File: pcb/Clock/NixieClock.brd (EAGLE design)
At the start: 108.4 x 46.5 mm, 47 parts, among them IC1 74141N, IC2 MEGA8-P, IC3 7805L, J1 DC-8N, Q1 IRF710, Q2 32kHz

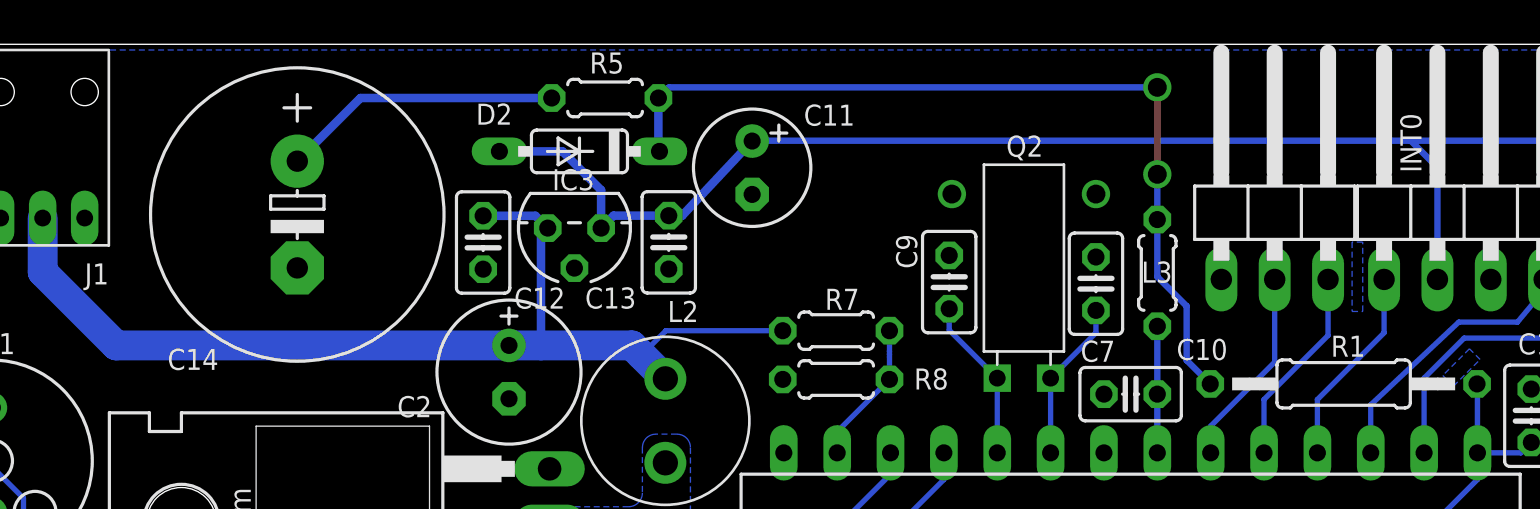
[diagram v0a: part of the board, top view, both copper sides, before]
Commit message: Replaced backup capacitor with a CR1220 battery holder.
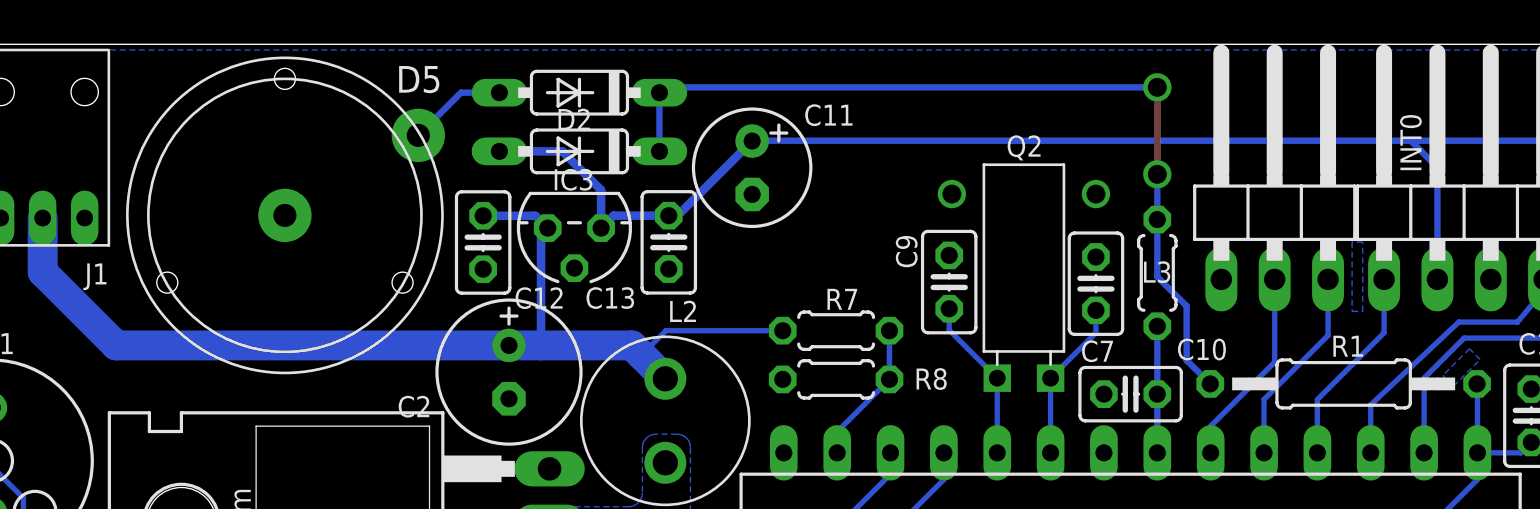
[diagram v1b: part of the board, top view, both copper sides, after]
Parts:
- removed C14: 0.1F, rcl:E5-13
- removed R5: 100, rcl:0204/5
- added D5: BAT85, diode:DO35-7
- added U$3: BAT1220THT, WB:1220
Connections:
- net GND: now also U$3.-; no longer C14.-
- net N$3: now also D5.A, U$3.+; no longer C14.+, R5.1
- net UC_VCC: now also D5.C; no longer R5.2
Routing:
- net N$3: track 13.4 -> 4.70 mm
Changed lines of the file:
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@@
 <?xml version="1.0" encoding="utf-8"?>
 <!DOCTYPE eagle SYSTEM "eagle.dtd">
-<eagle version="6.3">
+<eagle version="6.6.0">
 <drawing>
 <settings>
@@
 <attribute name="VALUE" x="50.927" y="45.847" size="1" layer="27" ratio="10" rot="R270"/>
 </element>
-<element name="C14" library="rcl" package="E5-13" value="0.1F" x="22.687" y="46.7775" smashed="yes" rot="R270">
-<attribute name="NAME" x="18.9391" y="40.3812" size="1" layer="25" ratio="10" rot="R180"/>
-<attribute name="VALUE" x="18.75" y="51.3495" size="1" layer="27" ratio="10" rot="R270"/>
-</element>
 <element name="D2" library="diode" package="DO35-7" value="BAT85" x="36.1188" y="49.784" smashed="yes" rot="R180">
-<attribute name="NAME" x="31.1912" y="51.054" size="1" layer="25" ratio="10"/>
+<attribute name="NAME" x="35.0012" y="50.8" size="1" layer="25" ratio="10"/>
 <attribute name="VALUE" x="34.5694" y="54.4322" size="1" layer="27" ratio="10" rot="R180"/>
 </element>
@@
 <attribute name="NAME" x="23.1394" y="28.321" size="1" layer="25" ratio="10" rot="R90"/>
 <attribute name="VALUE" x="25.8064" y="28.194" size="1" layer="27" ratio="10" rot="R90"/>
-</element>
-<element name="R5" library="rcl" package="0204/5" value="100" x="37.338" y="52.324" smashed="yes">
-<attribute name="NAME" x="36.6014" y="53.4924" size="1" layer="25" ratio="10"/>
-<attribute name="VALUE" x="35.2044" y="50.0126" size="1" layer="27" ratio="10"/>
 </element>
 <element name="C5" library="Various" package="CAP_RADIAL" value="4.7uF/250V" x="22.352" y="18.034" smashed="yes" rot="R180"/>
@@
 </element>
 <element name="R9" library="rcl" package="0204/5" value="10" x="40.132" y="29.591"/>
+<element name="U$3" library="WB" package="1220" value="BAT1220THT" x="22.098" y="46.736" rot="R180"/>
+<element name="D5" library="diode" package="DO35-7" value="BAT85" x="36.1188" y="52.578" smashed="yes" rot="R180">
+<attribute name="NAME" x="27.3812" y="52.578" size="1.27" layer="25" ratio="10"/>
+<attribute name="VALUE" x="38.4048" y="55.245" size="1.27" layer="27" ratio="10" rot="R180"/>
+</element>
 </elements>
 <signals>
@@
 <wire x1="40.3705" y1="46.7236" x2="37.7417" y2="46.7236" width="0.4064" layer="16"/>
 <wire x1="37.7417" y1="46.7236" x2="37.1497" y2="46.1316" width="0.4064" layer="16"/>
-<wire x1="75.692" y1="50.292" x2="44.3226" y2="50.292" width="0.3048" layer="16"/>
-<wire x1="41.0082" y1="46.7236" x2="40.3705" y2="46.7236" width="0.4064" layer="16"/>
+<wire x1="75.692" y1="50.292" x2="44.3576" y2="50.292" width="0.3048" layer="16"/>
 <wire x1="37.1497" y1="46.1316" x2="37.1497" y2="47.9403" width="0.4064" layer="16"/>
 <wire x1="37.1497" y1="47.9403" x2="35.306" y2="49.784" width="0.4064" layer="16"/>
 <wire x1="35.306" y1="49.784" x2="32.3088" y2="49.784" width="0.4064" layer="16"/>
 <wire x1="89.281" y1="34.163" x2="86.741" y2="34.163" width="0.3048" layer="16"/>
-<wire x1="44.3226" y1="50.292" x2="44.3405" y2="50.2749" width="0.4064" layer="16"/>
-<wire x1="41.0082" y1="46.7236" x2="44.3405" y2="50.2749" width="0.4064" layer="16"/>
 <wire x1="84.6836" y1="28.321" x2="85.1916" y2="27.813" width="0.4064" layer="16"/>
 <wire x1="85.1916" y1="27.813" x2="88.011" y2="27.813" width="0.3048" layer="16"/>
@@
 <wire x1="83.9724" y1="23.876" x2="83.9724" y2="21.5392" width="0.3048" layer="16"/>
 <wire x1="83.9724" y1="21.5392" x2="84.074" y2="21.4376" width="0.3048" layer="16"/>
+<wire x1="44.3576" y1="50.292" x2="44.3405" y2="50.2749" width="0.3048" layer="16"/>
+<wire x1="40.3705" y1="46.7236" x2="40.7892" y2="46.7236" width="0.4064" layer="16"/>
+<wire x1="40.7892" y1="46.7236" x2="44.3405" y2="50.2749" width="0.4064" layer="16"/>
 </signal>
 <signal name="GND">
@@
 <contactref element="C4" pad="2"/>
 <contactref element="C11" pad="-"/>
-<contactref element="C14" pad="-"/>
 <wire x1="63.627" y1="24.765" x2="63.627" y2="27.813" width="0.6096" layer="16"/>
 <wire x1="63.627" y1="21.844" x2="63.627" y2="24.765" width="0.6096" layer="16"/>
@@
 <contactref element="D4" pad="A"/>
 <contactref element="R3" pad="1"/>
+<contactref element="U$3" pad="-"/>
 </signal>
 <signal name="N$10">
@@
 <contactref element="D2" pad="C"/>
 <contactref element="R1" pad="2"/>
-<contactref element="R5" pad="2"/>
-<wire x1="63.627" y1="52.832" x2="40.386" y2="52.832" width="0.3048" layer="16"/>
-<wire x1="40.386" y1="52.832" x2="39.878" y2="52.324" width="0.3048" layer="16"/>
-<wire x1="39.878" y1="52.324" x2="39.878" y2="50.0888" width="0.4064" layer="16"/>
-<wire x1="39.878" y1="50.0888" x2="39.9288" y2="49.784" width="0.4064" layer="16"/>
+<wire x1="63.627" y1="52.832" x2="40.1828" y2="52.832" width="0.3048" layer="16"/>
 <wire x1="63.6272" y1="46.5383" x2="63.6272" y2="43.8148" width="0.3048" layer="16"/>
 <wire x1="65.024" y1="39.8368" x2="65.024" y2="42.418" width="0.3048" layer="16"/>
@@
 <wire x1="63.627" y1="48.6918" x2="63.627" y2="52.832" width="0.3048" layer="1"/>
 <via x="63.627" y="52.832" extent="1-16" drill="0.9"/>
+<contactref element="D5" pad="C"/>
+<wire x1="40.1828" y1="52.832" x2="39.9288" y2="52.578" width="0.3048" layer="16"/>
+<wire x1="39.9288" y1="49.784" x2="39.9288" y2="52.578" width="0.3048" layer="16"/>
 </signal>
 <signal name="ANODE2">
@@
 <wire x1="48.387" y1="36.4404" x2="48.387" y2="35.433" width="0.254" layer="16"/>
 </signal>
-<signal name="N$3">
-<contactref element="R5" pad="1"/>
-<contactref element="C14" pad="+"/>
-<wire x1="34.798" y1="52.324" x2="25.6935" y2="52.324" width="0.4064" layer="16"/>
-<wire x1="25.6935" y1="52.324" x2="22.687" y2="49.3175" width="0.4064" layer="16"/>
-</signal>
 <signal name="RXD">
 <contactref element="IC2" pad="2"/>
@@
 <wire x1="37.592" y1="27.178" x2="37.592" y2="29.591" width="0.4064" layer="16"/>
 </signal>
+<signal name="N$3">
+<contactref element="U$3" pad="+"/>
+<contactref element="D5" pad="A"/>
+<wire x1="32.3088" y1="52.578" x2="30.48" y2="52.578" width="0.3048" layer="16"/>
+<wire x1="30.48" y1="52.578" x2="28.448" y2="50.546" width="0.3048" layer="16"/>
+</signal>
 </signals>

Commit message: Changed MOSFET from IRF710 to IRF740. Added part number for inductor
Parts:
- L2: value 330uH -> DLCW330 300uH/0.4A
- Q1: value IRF710 -> IRF740
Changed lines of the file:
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@@
 <attribute name="VALUE" x="17.4752" y="20.0152" size="1" layer="27" ratio="10" rot="R180"/>
 </element>
-<element name="L2" library="WB" package="MURATA-CHOKE-7-4" value="330uH" x="40.2082" y="36.957" smashed="yes" rot="R270">
+<element name="L2" library="WB" package="MURATA-CHOKE-7-4" value="DLCW330 300uH/0.4A" x="40.2082" y="36.957" smashed="yes" rot="R270">
 <attribute name="NAME" x="40.315" y="41.6602" size="1" layer="21"/>
 </element>
-<element name="Q1" library="transistor-power" package="TO220BH" value="IRF710" x="28.3464" y="32.131" smashed="yes" rot="R90">
+<element name="Q1" library="transistor-power" package="TO220BH" value="IRF740" x="28.3464" y="32.131" smashed="yes" rot="R90">
 <attribute name="NAME" x="23.1394" y="28.321" size="1" layer="25" ratio="10" rot="R90"/>
 <attribute name="VALUE" x="25.8064" y="28.194" size="1" layer="27" ratio="10" rot="R90"/>

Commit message: Added part number for photoresistor
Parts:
- JP2: value PHOTO_SENSOR -> LDR07 50K
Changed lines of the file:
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@@
 <attribute name="NAME" x="56.4339" y="49.5302" size="1" layer="21"/>
 </element>
-<element name="JP2" library="pinhead" package="1X02" value="PHOTO_SENSOR" x="80.5434" y="19.5834" smashed="yes" rot="R270">
+<element name="JP2" library="pinhead" package="1X02" value="LDR07 50K" x="80.5434" y="19.5834" smashed="yes" rot="R270">
 <attribute name="NAME" x="82.4992" y="20.6756" size="1" layer="25" ratio="10" rot="R270"/>
 <attribute name="VALUE" x="77.3684" y="22.1234" size="1" layer="27" rot="R270"/>
